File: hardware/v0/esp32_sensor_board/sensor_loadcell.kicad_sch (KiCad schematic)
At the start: 9 parts, among them J501 Conn_01x05, J502 Conn_01x05

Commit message: Clean up errors
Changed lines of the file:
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@@
+    (effects (font (size 1.27 1.27)) (justify left bottom))
+  )
+  (label "S2_P" (at 45.72 177.8 0) (fields_autoplaced)
+    (effects (font (size 1.27 1.27)) (justify left bottom))
+  )
+  (label "S1_N" (at 60.96 167.64 0) (fields_autoplaced)
+    (effects (font (size 1.27 1.27)) (justify left bottom))
+  )
+  (label "SHIELD" (at 48.26 116.84 0) (fields_autoplaced)
+    (effects (font (size 1.27 1.27)) (justify left bottom))
+  )
+  (label "S2_N" (at 48.26 111.76 0) (fields_autoplaced)
+    (effects (font (size 1.27 1.27)) (justify left bottom))
+  )
+  (label "S1_P" (at 48.26 93.98 0) (fields_autoplaced)
+    (effects (font (size 1.27 1.27)) (justify left bottom))
+  )
+  (label "E_n" (at 48.26 88.9 0) (fields_autoplaced)
+    (effects (font (size 1.27 1.27)) (justify left bottom))
+  )
+  (label "S2_N" (at 93.98 104.14 180) (fields_autoplaced)
+    (effects (font (size 1.27 1.27)) (justify right bottom))
+  )
+  (label "SHIELD" (at 73.66 55.88 180) (fields_autoplaced)
+    (effects (font (size 1.27 1.27)) (justify right bottom))
+  )
+  (label "S1_P" (at 93.98 96.52 180) (fields_autoplaced)
+    (effects (font (size 1.27 1.27)) (justify right bottom))
+  )
+  (label "E_p" (at 93.98 88.9 180) (fields_autoplaced)
+    (effects (font (size 1.27 1.27)) (justify right bottom))
+  )
+  (label "S2_P" (at 48.26 114.3 0) (fields_autoplaced)
+    (effects (font (size 1.27 1.27)) (justify left bottom))
+  )
+  (label "S1_N" (at 48.26 91.44 0) (fields_autoplaced)
+    (effects (font (size 1.27 1.27)) (justify left bottom))
+  )
+  (label "S1_N" (at 93.98 93.98 180) (fields_autoplaced)
+    (effects (font (size 1.27 1.27)) (justify right bottom))
+  )
+  (label "E_n" (at 144.78 99.06 0) (fields_autoplaced)
+    (effects (font (size 1.27 1.27)) (justify left bottom))
+  )
+  (label "E_n" (at 58.42 55.88 180) (fields_autoplaced)
+    (effects (font (size 1.27 1.27)) (justify right bottom))
+  )
+  (label "S1_P" (at 60.96 177.8 0) (fields_autoplaced)
+    (effects (font (size 1.27 1.27)) (justify left bottom))
+  )
+  (label "E_p" (at 48.26 86.36 0) (fields_autoplaced)
+    (effects (font (size 1.27 1.27)) (justify left bottom))
+  )
+  (label "E_p" (at 25.4 55.88 180) (fields_autoplaced)
+    (effects (font (size 1.27 1.27)) (justify right bottom))
+  )
+  (label "E_n" (at 48.26 109.22 0) (fields_autoplaced)
+    (effects (font (size 1.27 1.27)) (justify left bottom))
+  )
+  (label "E_p" (at 48.26 106.68 0) (fields_autoplaced)
+    (effects (font (size 1.27 1.27)) (justify left bottom))
+  )
+  (label "S2_P" (at 93.98 106.68 180) (fields_autoplaced)
+    (effects (font (size 1.27 1.27)) (justify right bottom))
+  )
+  (label "S2_N" (at 45.72 167.64 0) (fields_autoplaced)
+    (effects (font (size 1.27 1.27)) (justify left bottom))
+  )
+  (label "SHIELD" (at 48.26 96.52 0) (fields_autoplaced)
     (effects (font (size 1.27 1.27)) (justify left bottom))
   )
@@
     (effects (font (size 1.27 1.27)) (justify left))
   )
-  (hierarchical_label "S1_N" (shape input) (at 93.98 93.98 180) (fields_autoplaced)
-    (effects (font (size 1.27 1.27)) (justify right))
-  )
-  (hierarchical_label "E_n" (shape input) (at 144.78 99.06 0) (fields_autoplaced)
-    (effects (font (size 1.27 1.27)) (justify left))
-  )
-  (hierarchical_label "S1_N" (shape input) (at 60.96 167.64 0) (fields_autoplaced)
-    (effects (font (size 1.27 1.27)) (justify left))
-  )
   (hierarchical_label "SCK" (shape input) (at 134.62 91.44 0) (fields_autoplaced)
-    (effects (font (size 1.27 1.27)) (justify left))
-  )
-  (hierarchical_label "S2_N" (shape input) (at 48.26 111.76 0) (fields_autoplaced)
-    (effects (font (size 1.27 1.27)) (justify left))
-  )
-  (hierarchical_label "S2_N" (shape input) (at 45.72 167.64 0) (fields_autoplaced)
-    (effects (font (size 1.27 1.27)) (justify left))
-  )
-  (hierarchical_label "S2_N" (shape input) (at 93.98 104.14 180) (fields_autoplaced)
-    (effects (font (size 1.27 1.27)) (justify right))
-  )
-  (hierarchical_label "SHIELD" (shape input) (at 48.26 96.52 0) (fields_autoplaced)
-    (effects (font (size 1.27 1.27)) (justify left))
-  )
-  (hierarchical_label "E_p" (shape input) (at 48.26 106.68 0) (fields_autoplaced)
     (effects (font (size 1.27 1.27)) (justify left))
   )
@@
     (effects (font (size 1.27 1.27)) (justify left))
   )
-  (hierarchical_label "E_n" (shape input) (at 58.42 55.88 180) (fields_autoplaced)
-    (effects (font (size 1.27 1.27)) (justify right))
-  )
-  (hierarchical_label "E_n" (shape input) (at 48.26 88.9 0) (fields_autoplaced)
-    (effects (font (size 1.27 1.27)) (justify left))
-  )
-  (hierarchical_label "S1_N" (shape input) (at 48.26 91.44 0) (fields_autoplaced)
-    (effects (font (size 1.27 1.27)) (justify left))
-  )
-  (hierarchical_label "E_p" (shape input) (at 25.4 55.88 180) (fields_autoplaced)
-    (effects (font (size 1.27 1.27)) (justify right))
-  )
-  (hierarchical_label "S1_P" (shape input) (at 93.98 96.52 180) (fields_autoplaced)
-    (effects (font (size 1.27 1.27)) (justify right))
-  )
-  (hierarchical_label "S2_P" (shape input) (at 45.72 177.8 0) (fields_autoplaced)
-    (effects (font (size 1.27 1.27)) (justify left))
-  )
-  (hierarchical_label "S2_P" (shape input) (at 93.98 106.68 180) (fields_autoplaced)
-    (effects (font (size 1.27 1.27)) (justify right))
-  )
   (hierarchical_label "SDA" (shape input) (at 134.62 88.9 0) (fields_autoplaced)
     (effects (font (size 1.27 1.27)) (justify left))
   )
-  (hierarchical_label "E_p" (shape input) (at 93.98 88.9 180) (fields_autoplaced)
-    (effects (font (size 1.27 1.27)) (justify right))
-  )
-  (hierarchical_label "S1_P" (shape input) (at 48.26 93.98 0) (fields_autoplaced)
-    (effects (font (size 1.27 1.27)) (justify left))
-  )
-  (hierarchical_label "E_n" (shape input) (at 48.26 109.22 0) (fields_autoplaced)
-    (effects (font (size 1.27 1.27)) (justify left))
-  )
-  (hierarchical_label "E_p" (shape input) (at 48.26 86.36 0) (fields_autoplaced)
-    (effects (font (size 1.27 1.27)) (justify left))
-  )
-  (hierarchical_label "SHIELD" (shape input) (at 73.66 55.88 180) (fields_autoplaced)
-    (effects (font (size 1.27 1.27)) (justify right))
-  )
-  (hierarchical_label "S2_P" (shape input) (at 48.26 114.3 0) (fields_autoplaced)
-    (effects (font (size 1.27 1.27)) (justify left))
-  )
-  (hierarchical_label "SHIELD" (shape input) (at 48.26 116.84 0) (fields_autoplaced)
-    (effects (font (size 1.27 1.27)) (justify left))
-  )
-  (hierarchical_label "S1_P" (shape input) (at 60.96 177.8 0) (fields_autoplaced)
-    (effects (font (size 1.27 1.27)) (justify left))
-  )

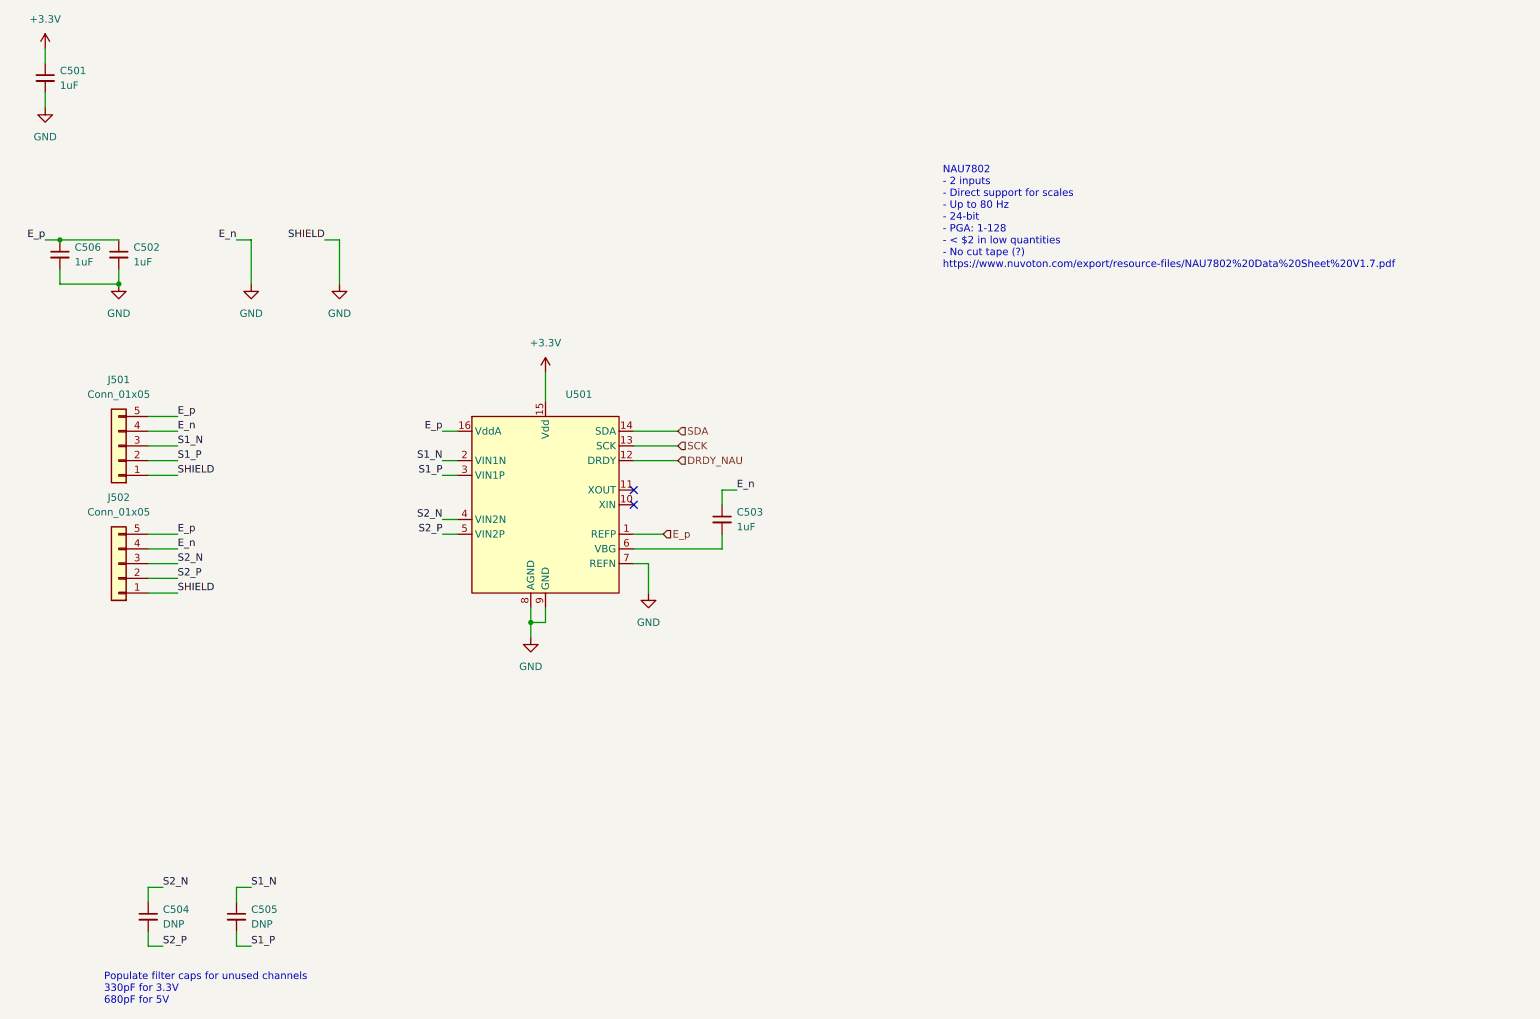
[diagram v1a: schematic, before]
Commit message: PCB ordered, a few initial mistakes fixed
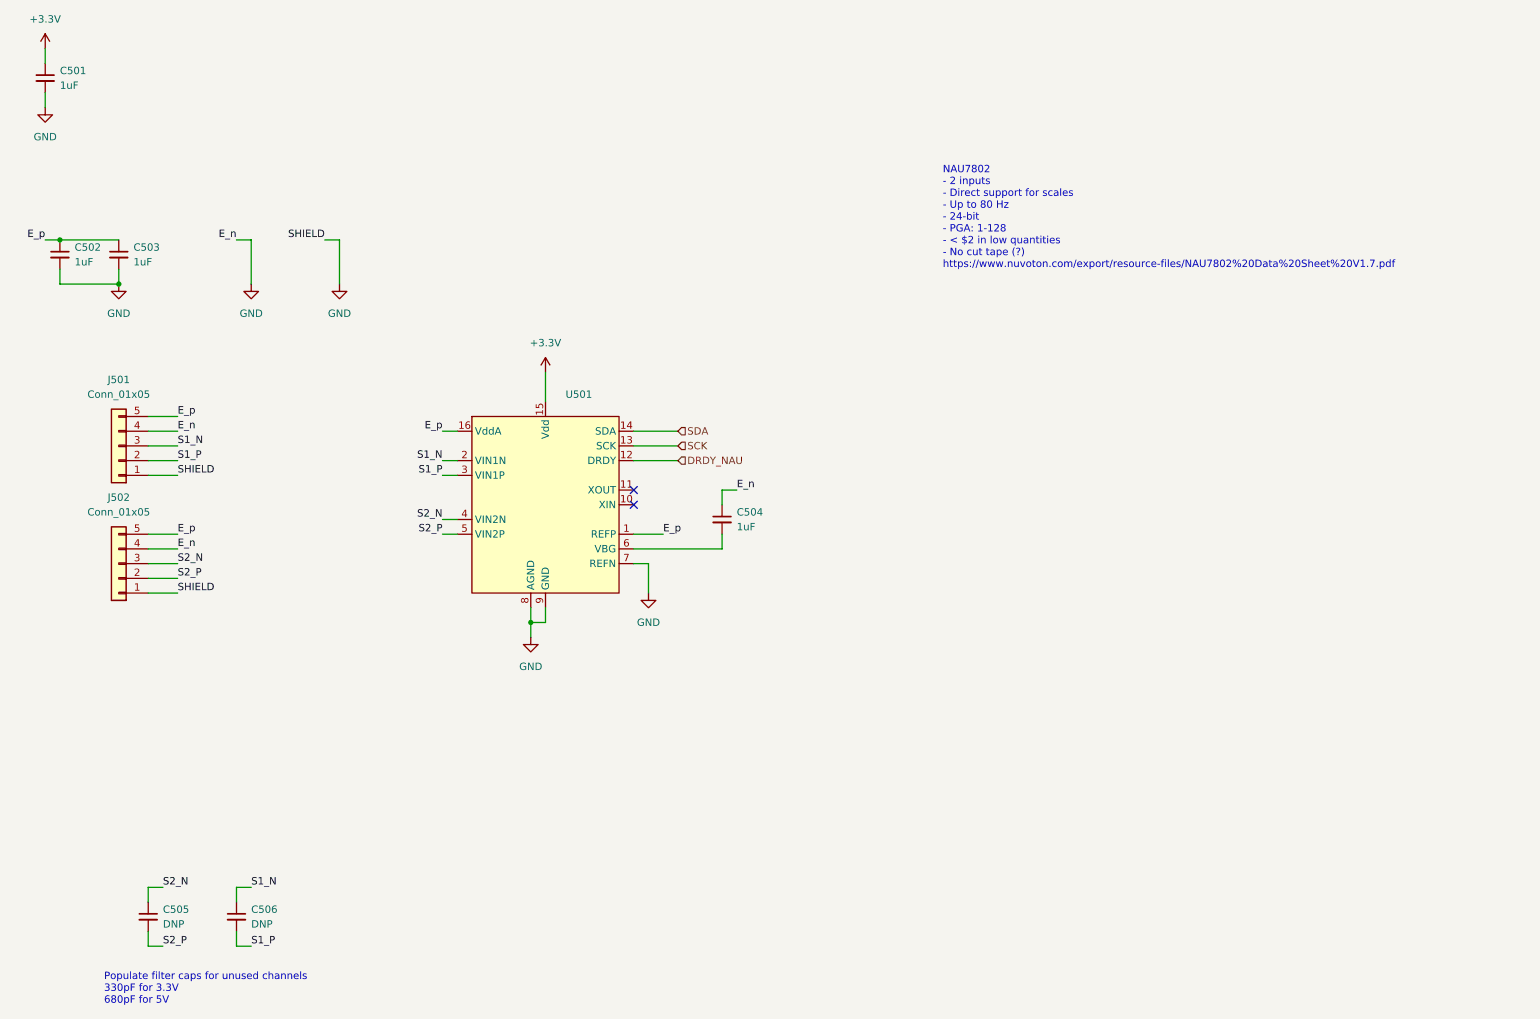
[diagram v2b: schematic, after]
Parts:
- J501, J502: footprint (none) -> Connector_PinHeader_2.54mm:PinHeader_1x05_P2.54mm_Horizontal
- renumbered C506 to C502, C502 to C503, C503 to C504, C504 to C505, C505 to C506
